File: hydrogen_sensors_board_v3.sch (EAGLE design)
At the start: 79 parts, among them CN1 1X4-CLEANBIG, IC1 317T, IC2 LM741D, U1 ATMEGA328P_TQFP, Y1 16MHz

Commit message: Added decoupling caps and inductor
100nF cap moved closer to VCC pin on right side of ATmega, added
inductor on AVCC line which then connects to 5V line. This is for more
accurate ADC measurements as noted in datasheet. 100nF cap also added to
12V line for decoupling.
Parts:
- added C16: 100nF, adafruit:C-USC0603
- added L1: 100uH, SparkFun:INDUCTOR0603
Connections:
- new net N$6: L1.2, U1.AVCC
- net +12V: now also C16.1
- net +5V: now also L1.1; no longer U1.AVCC
- net GND: now also C16.2
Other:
- note added: "Added 7 segment display pads for live H2 reading and error code display"
- note added: "Cleaned up schematic Added 100nF cap to ground on AREF pin on ATMega, added other decoupling caps around ATMega, added inductor on AVCC pin, added 100nF decoupling cap on 12V line"
- note added: "Google "LM317 resistor calculator" for how resistor values were calculated."
- note removed: "Added 7 segment display pads and associated I2C connections"
- note removed: "Cleaned up schematic Added 100nF cap to ground on AREF pin on ATMega"
- note removed: "Google "LM317 resistor calculator" for resistor values."
- moved on the sheet: C3, C4, C5, C6

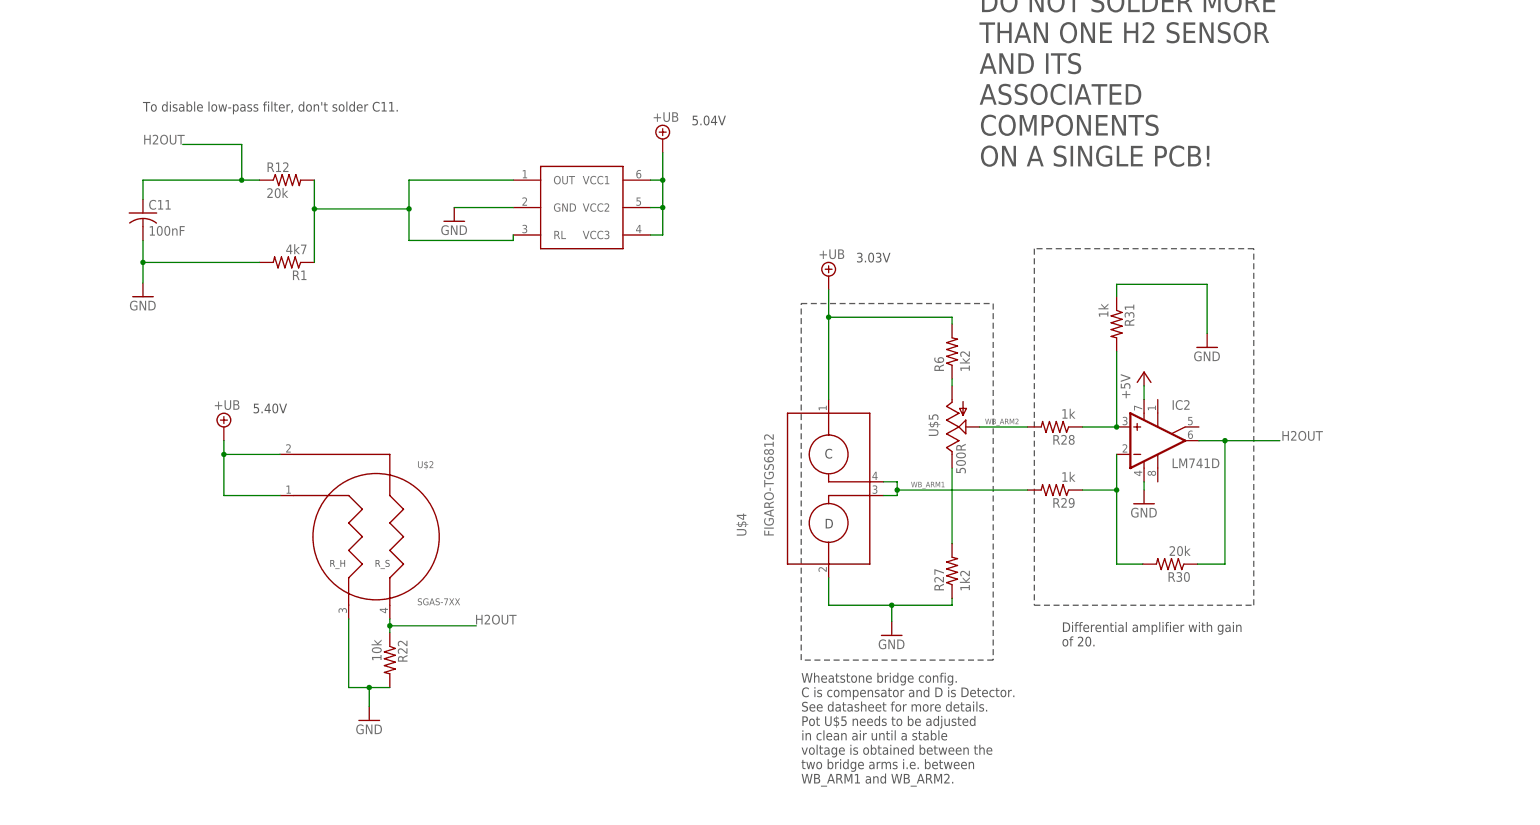
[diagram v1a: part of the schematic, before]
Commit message: Noise filtering, R_s sensor voltage updated, updated README, brd and sch cleaned up
Noise filtering
Added low-pass filters to IDT SGAS and Figaro sensors.

R_s sensor voltage updated
IDT SGAS sensor's R_s voltage changed to 5V Vcc from 5.4V Regulator
output (Ub). Datasheet says max permitted voltage for R_s is 5V.

Updated README
Links to preliminary documentation and folder on Gdrive with other
files.

brd and sch cleaned up
Buttons moved a bit to the left, MQ-8 sensor schematic mirrored to match
other sensors.
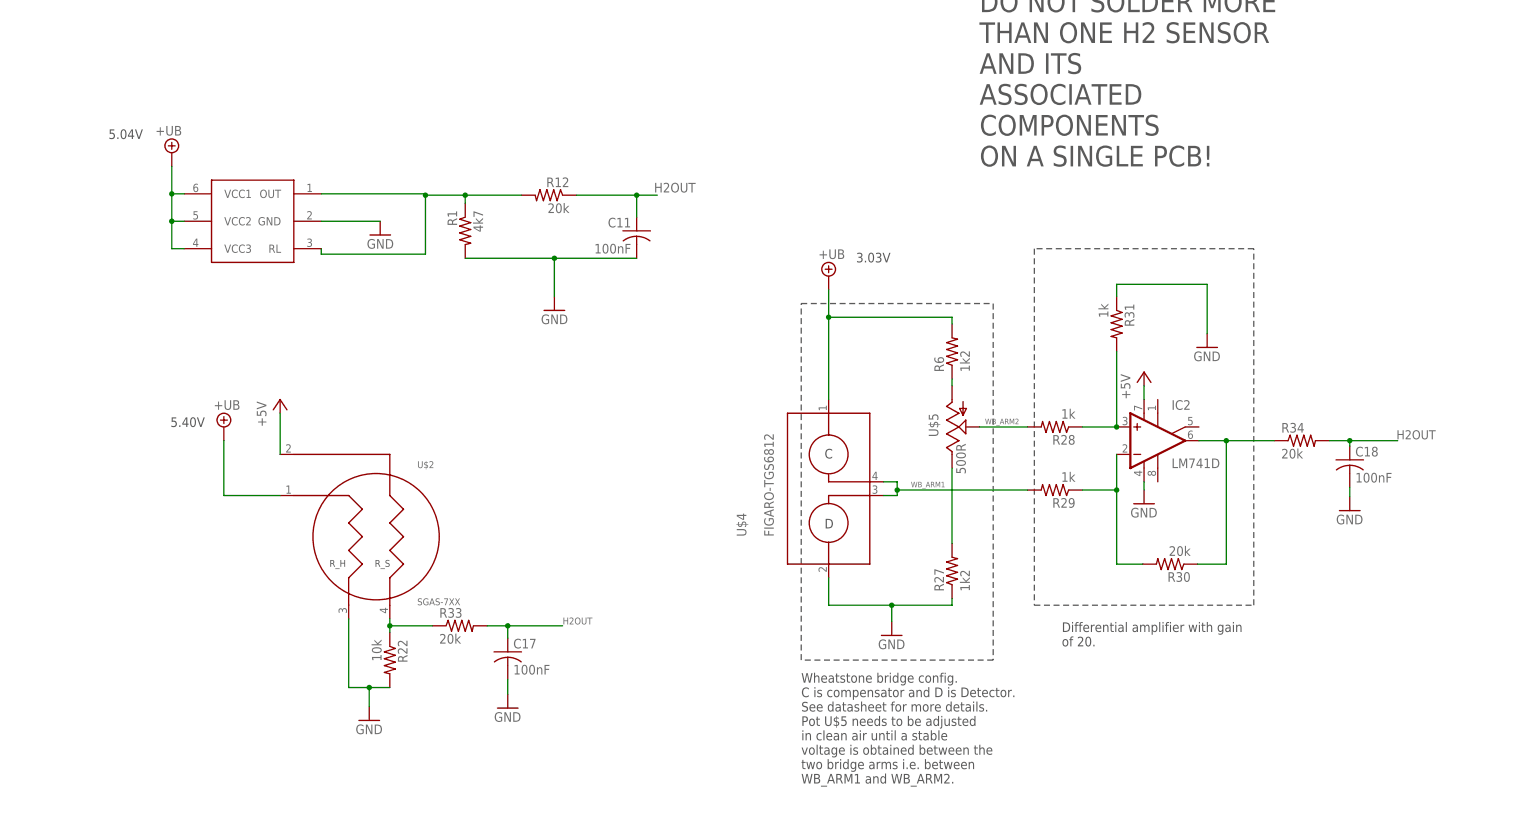
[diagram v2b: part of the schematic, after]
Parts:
- added C17, C18: 100nF, adafruit:C-USC0603
- added R33, R34: 20k, SparkFun-Passives:RESISTOR0603-RES
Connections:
- new net N$20: IC2.OUT, R30.1, R34.1
- new net N$5: R22.1, R33.1, U$2.4
- net +5V: now also U$2.2
- net +UB: no longer U$2.2
- net GND: now also C17.2, C18.2
- net H2OUT: now also C17.1, C18.1, R33.2, R34.2; no longer IC2.OUT, R22.1, R30.1, U$2.4
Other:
- note removed: "To disable low-pass filter, don't solder C11."
- moved on the sheet: C11, R1, R12

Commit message: Inductor value, multimeter probe points, README
Inductor value
Changed inductor value on MCU AVCC pin to 10uH per datasheet
recommendation.

Multimeter probe points
Added two probe points for the two arms of the Wheatstone bridge for the
Figaro H2 sensor circuit. Will make it easy to measure voltage between
the two arms when adjusting the potentiometer in clean air.

README
Updated links and heading in README.
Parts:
- L1: value 100uH -> 10uH
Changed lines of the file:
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@@
 <part name="C15" library="adafruit" deviceset="C-US" device="C0603" value="100nF"/>
 <part name="GND29" library="SparkFun" deviceset="GND" device=""/>
-<part name="L1" library="SparkFun" deviceset="INDUCTOR" device="0603" value="100uH"/>
+<part name="L1" library="SparkFun" deviceset="INDUCTOR" device="0603" value="10uH"/>
 <part name="C16" library="adafruit" deviceset="C-US" device="C0603" value="100nF"/>
 <part name="GND30" library="supply1" deviceset="GND" device=""/>

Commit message: Added more decoupling caps
Added 100uF electrolytic, through-hole caps to regulator input and output. These caps are in addition to the ceramic and tantalum caps already present. Also added one more 100nF cap near the MCU.
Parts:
- added C19, C20: 100uF, SparkFun-Capacitors:CAP_POLPTH1
- added C21: 100nF, adafruit:C-USC0603
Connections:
- net +12V: now also C20.+
- net +5V: now also C21.1
- net +UB: now also C19.+
- net GND: now also C19.-, C20.-, C21.2
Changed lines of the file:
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@@
 <part name="GND31" library="supply1" deviceset="GND" device=""/>
 <part name="GND32" library="supply1" deviceset="GND" device=""/>
+<part name="C19" library="SparkFun-Capacitors" deviceset="CAP_POL" device="PTH1" value="100uF"/>
+<part name="C20" library="SparkFun-Capacitors" deviceset="CAP_POL" device="PTH1" value="100uF"/>
+<part name="C21" library="adafruit" deviceset="C-US" device="C0603" value="100nF"/>
 </parts>
 <sheets>
@@
 ESTOP1, ESTOP2, H2GasConc_OK, and RemoteKill signals all get ANDED into one
 H2_OK_3V3 signal which is sent to the FCC.</text>
-<wire x1="15.24" y1="388.62" x2="15.24" y2="256.54" width="1.016" layer="150"/>
-<wire x1="15.24" y1="256.54" x2="180.34" y2="256.54" width="1.016" layer="150"/>
+<wire x1="10.16" y1="388.62" x2="10.16" y2="256.54" width="1.016" layer="150"/>
+<wire x1="10.16" y1="256.54" x2="180.34" y2="256.54" width="1.016" layer="150"/>
 <wire x1="180.34" y1="256.54" x2="180.34" y2="388.62" width="1.016" layer="150"/>
-<wire x1="180.34" y1="388.62" x2="15.24" y2="388.62" width="1.016" layer="150"/>
+<wire x1="180.34" y1="388.62" x2="10.16" y2="388.62" width="1.016" layer="150"/>
 <wire x1="15.24" y1="187.96" x2="274.32" y2="187.96" width="1.016" layer="150"/>
 <wire x1="274.32" y1="187.96" x2="274.32" y2="30.48" width="1.016" layer="150"/>
 <wire x1="274.32" y1="30.48" x2="15.24" y2="30.48" width="1.016" layer="150"/>
 <wire x1="15.24" y1="30.48" x2="15.24" y2="187.96" width="1.016" layer="150"/>
-<wire x1="347.98" y1="408.94" x2="347.98" y2="256.54" width="1.016" layer="150"/>
-<wire x1="347.98" y1="256.54" x2="543.56" y2="256.54" width="1.016" layer="150"/>
+<wire x1="340.36" y1="408.94" x2="340.36" y2="256.54" width="1.016" layer="150"/>
+<wire x1="340.36" y1="256.54" x2="543.56" y2="256.54" width="1.016" layer="150"/>
 <wire x1="543.56" y1="256.54" x2="543.56" y2="408.94" width="1.016" layer="150"/>
-<wire x1="543.56" y1="408.94" x2="347.98" y2="408.94" width="1.016" layer="150"/>
+<wire x1="543.56" y1="408.94" x2="340.36" y2="408.94" width="1.016" layer="150"/>
 <wire x1="322.58" y1="203.2" x2="322.58" y2="58.42" width="1.016" layer="150"/>
 <wire x1="322.58" y1="58.42" x2="548.64" y2="58.42" width="1.016" layer="150"/>
@@
 <instance part="GND17" gate="1" x="76.2" y="295.656"/>
 <instance part="C12" gate="G$1" x="77.47" y="349.25"/>
-<instance part="GND18" gate="1" x="82.55" y="339.852"/>
+<instance part="GND18" gate="1" x="86.868" y="339.852"/>
 <instance part="C13" gate="G$1" x="30.48" y="346.71"/>
-<instance part="GND19" gate="1" x="25.4" y="337.058"/>
+<instance part="GND19" gate="1" x="21.082" y="337.058"/>
 <instance part="U$4" gate="G$1" x="154.94" y="88.9" smashed="yes">
 <attribute name="NAME" x="139.7" y="81.28" size="1.778" layer="95" rot="R90"/>
@@
 <instance part="GND31" gate="1" x="95.504" y="49.53"/>
 <instance part="GND32" gate="1" x="251.46" y="86.106"/>
+<instance part="C19" gate="G$1" x="97.028" y="349.504"/>
+<instance part="C20" gate="G$1" x="14.224" y="346.71"/>
+<instance part="C21" gate="G$1" x="345.44" y="314.96"/>
 </instances>
 <busses>
@@
 <wire x1="357.632" y1="327.66" x2="357.632" y2="323.088" width="0.1524" layer="91"/>
 <junction x="357.632" y="323.088"/>
+<pinref part="C21" gate="G$1" pin="1"/>
+<wire x1="353.06" y1="317.5" x2="345.44" y2="317.5" width="0.1524" layer="91"/>
+<junction x="353.06" y="317.5"/>
 </segment>
 <segment>
@@
 <junction x="357.632" y="309.88"/>
 <junction x="357.632" y="302.26"/>
+<pinref part="C21" gate="G$1" pin="2"/>
+<wire x1="353.06" y1="309.88" x2="345.44" y2="309.88" width="0.1524" layer="91"/>
+<junction x="353.06" y="309.88"/>
 </segment>
 <segment>
@@
 <pinref part="C10" gate="G$1" pin="-"/>
 <wire x1="86.868" y1="344.424" x2="86.868" y2="342.392" width="0.1524" layer="91"/>
-<wire x1="86.868" y1="342.392" x2="82.55" y2="342.392" width="0.1524" layer="91"/>
-<junction x="82.55" y="342.392"/>
-<wire x1="82.55" y1="342.392" x2="77.47" y2="342.392" width="0.1524" layer="91"/>
+<junction x="86.868" y="342.392"/>
+<wire x1="86.868" y1="342.392" x2="77.47" y2="342.392" width="0.1524" layer="91"/>
 <wire x1="77.47" y1="342.392" x2="77.47" y2="344.17" width="0.1524" layer="91"/>
+<pinref part="C19" gate="G$1" pin="-"/>
+<wire x1="97.028" y1="344.424" x2="97.028" y2="342.392" width="0.1524" layer="91"/>
+<wire x1="97.028" y1="342.392" x2="86.868" y2="342.392" width="0.1524" layer="91"/>
+<junction x="86.868" y="342.392"/>
 </segment>
 <segment>
@@
 <pinref part="GND19" gate="1" pin="GND"/>
 <pinref part="C14" gate="G$1" pin="-"/>
-<wire x1="25.4" y1="339.598" x2="21.082" y2="339.598" width="0.1524" layer="91"/>
 <wire x1="21.082" y1="339.598" x2="21.082" y2="341.63" width="0.1524" layer="91"/>
-<junction x="25.4" y="339.598"/>
-<wire x1="25.4" y1="339.598" x2="30.48" y2="339.598" width="0.1524" layer="91"/>
+<junction x="21.082" y="339.598"/>
+<wire x1="21.082" y1="339.598" x2="30.48" y2="339.598" width="0.1524" layer="91"/>
 <wire x1="30.48" y1="339.598" x2="30.48" y2="341.63" width="0.1524" layer="91"/>
+<pinref part="C20" gate="G$1" pin="-"/>
+<wire x1="14.224" y1="341.63" x2="14.224" y2="339.598" width="0.1524" layer="91"/>
+<wire x1="14.224" y1="339.598" x2="21.082" y2="339.598" width="0.1524" layer="91"/>
+<junction x="21.082" y="339.598"/>
 </segment>
 <segment>
@@
 <wire x1="30.48" y1="353.06" x2="21.082" y2="353.06" width="0.1524" layer="91"/>
 <wire x1="21.082" y1="353.06" x2="21.082" y2="349.25" width="0.1524" layer="91"/>
+<pinref part="C20" gate="G$1" pin="+"/>
+<wire x1="21.082" y1="353.06" x2="14.224" y2="353.06" width="0.1524" layer="91"/>
+<wire x1="14.224" y1="353.06" x2="14.224" y2="349.25" width="0.1524" layer="91"/>
+<junction x="21.082" y="353.06"/>
 </segment>
 <segment>
@@
 <wire x1="86.868" y1="353.06" x2="86.868" y2="352.044" width="0.1524" layer="91"/>
 <junction x="77.47" y="353.06"/>
-</segment>
-<segment>
+<pinref part="C19" gate="G$1" pin="+"/>
+<wire x1="86.868" y1="353.06" x2="97.028" y2="353.06" width="0.1524" layer="91"/>
+<wire x1="97.028" y1="353.06" x2="97.028" y2="352.044" width="0.1524" layer="91"/>
+<junction x="86.868" y="353.06"/>
+</segment>
+<segment>

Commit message: Decoupling caps, remote H2 sensor, MCU LC network, protection diodes, Figaro op-amp
- Decoupling caps
Added decoupling caps to H2 sensor inputs (100nF)

- Remote H2 sensor
Connected remote H2 sensor to MCU. Was disconnected previously. Also added pull-down resistor and low-pass filter

- MCU LC network
Corrected errors in LC network on AVcc pin of MCU. Capacitor was connected on Vcc side of inductor. It has now been connected to AVcc pin side of inductor as shown in the ATmega datasheet.

- Protection diodes
Added protection diodes to on-board regulator as per datasheet.

- Figaro op-amp
Corrected errors in Figaro H2 sensor's op-amp circuit. + and - lines were switched and R31 was switched to 20k
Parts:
- added C22, C23, C24, C25, C27: 100nF, adafruit:C-USC0603
- added D1, D2: S1GTR, adafruit:DIODESMA
- added R35: 1k, SparkFun-Passives:RESISTOR0603-RES
- added R36: 20k, SparkFun-Passives:RESISTOR0603-RES
- R31: value 1k -> 20k
- U$5: value 500R -> 100R
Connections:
- new net N$62: C21.1, L1.2, U1.AVCC
- net +12V: now also D1.C
- net +5V: now also C24.1; no longer C21.1
- net +UB: now also C22.1, C23.1, C25.1, D1.A, D2.C
- net GND: now also C22.2, C23.2, C24.2, C25.2, C27.2, R35.1
- net H2_REMOTE: now also R35.2, R36.1
- net N$13: now also R28.1; no longer R29.1
- net N$22: now also R29.1; no longer R28.1
- net N$6: now also C27.1, R36.2, U1.PD6(AIN0); no longer L1.2, U1.AVCC
- net V_ADJ: now also D2.A
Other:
- moved on the sheet: C21, C3, C6, IC2, L1, R30, R31, R7, S1

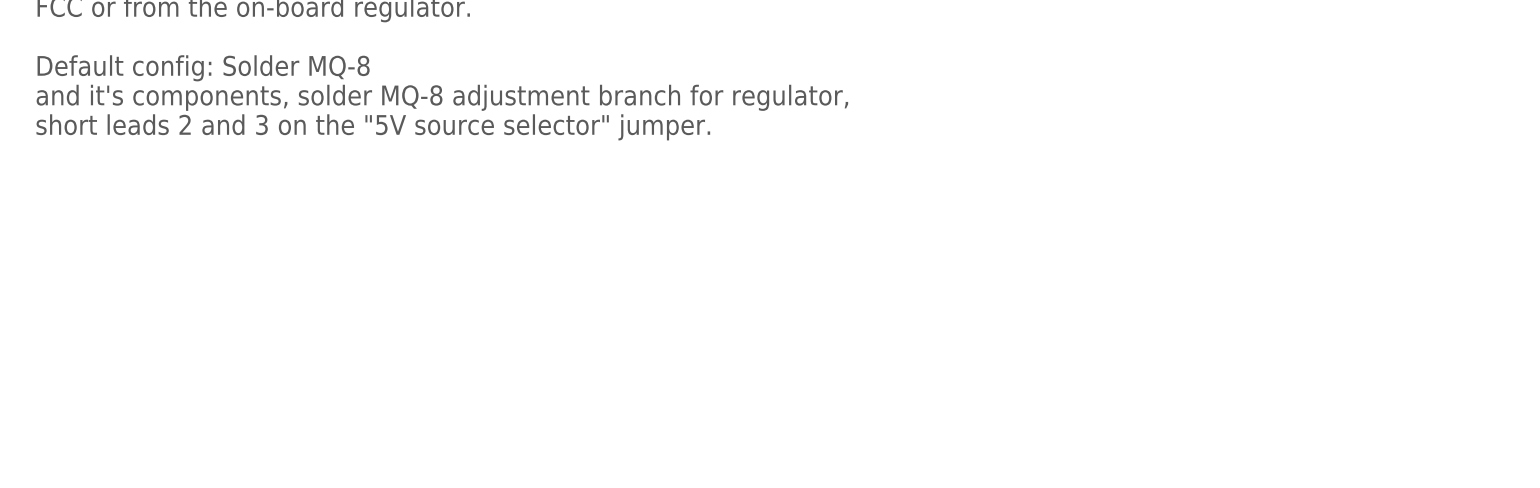
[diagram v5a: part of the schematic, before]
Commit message: Moved MQ-8 resistors and capacitor, updated change-log
Moved components a bit so that they don't overlap with the MQ-8 H2 sensor.

Updated changelog in .sch file
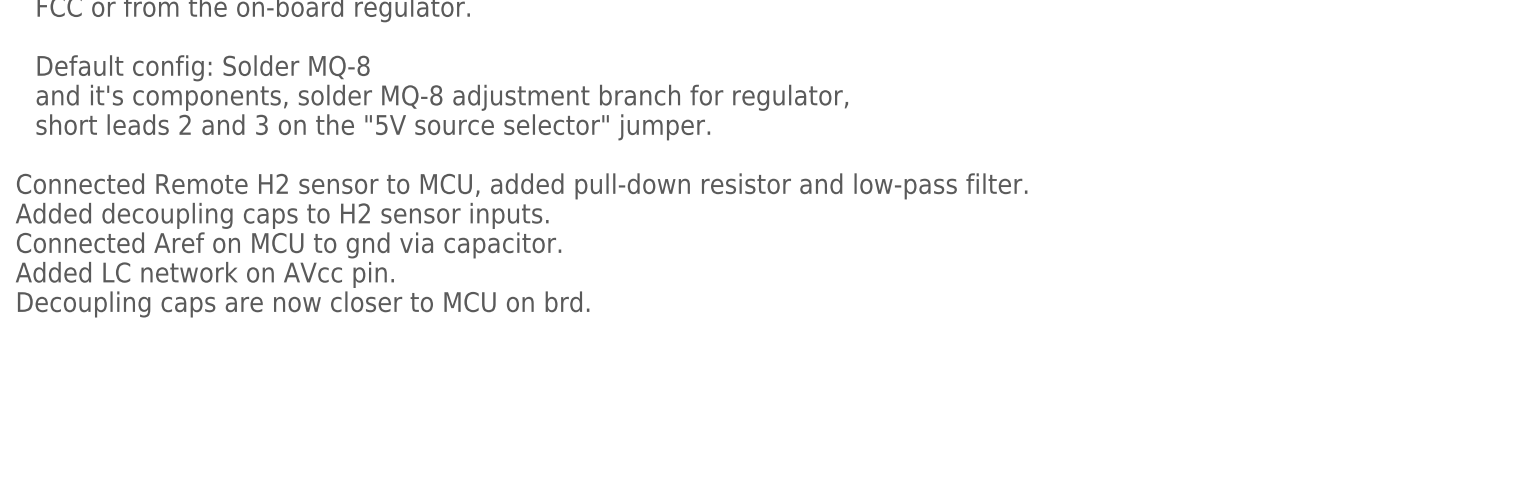
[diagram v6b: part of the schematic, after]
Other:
- note added: "Connected Remote H2 sensor to MCU, added pull-down resistor and low-pass filter. Added decoupling caps to H2 sensor inputs. Connected Aref on MCU to gnd via capacitor. Added LC network on AVcc pin. Decoupling caps are now closer to MCU on brd."
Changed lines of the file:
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@@
 or from the FCC ethernet connector.
 Default is from the on-board regulator.</text>
+<text x="-180.34" y="139.7" size="2.54" layer="97">Connected Remote H2 sensor to MCU, added pull-down resistor and low-pass filter.
+Added decoupling caps to H2 sensor inputs.
+Connected Aref on MCU to gnd via capacitor.
+Added LC network on AVcc pin.
+Decoupling caps are now closer to MCU on brd.</text>
 </plain>
 <instances>
